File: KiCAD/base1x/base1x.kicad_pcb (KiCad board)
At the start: 4 copper layers, 62.2 x 110 mm, 40 parts, among them J1 Conn_02x05_Odd_Even, J2 GS3, J3 Conn_02x14_Counter_Clockwise, J4 GS3, J6 Conn_02x14_Counter_Clockwise, J7 Conn_02x06_Counter_Clockwise, J8 Conn_02x06_Counter_Clockwise, J9 Screw_Terminal_01x08, P1 CONN_01X02, P2 CONN_01X02, P3 CONN_01X02, P4 CONN_01X02, U1 ADS1115

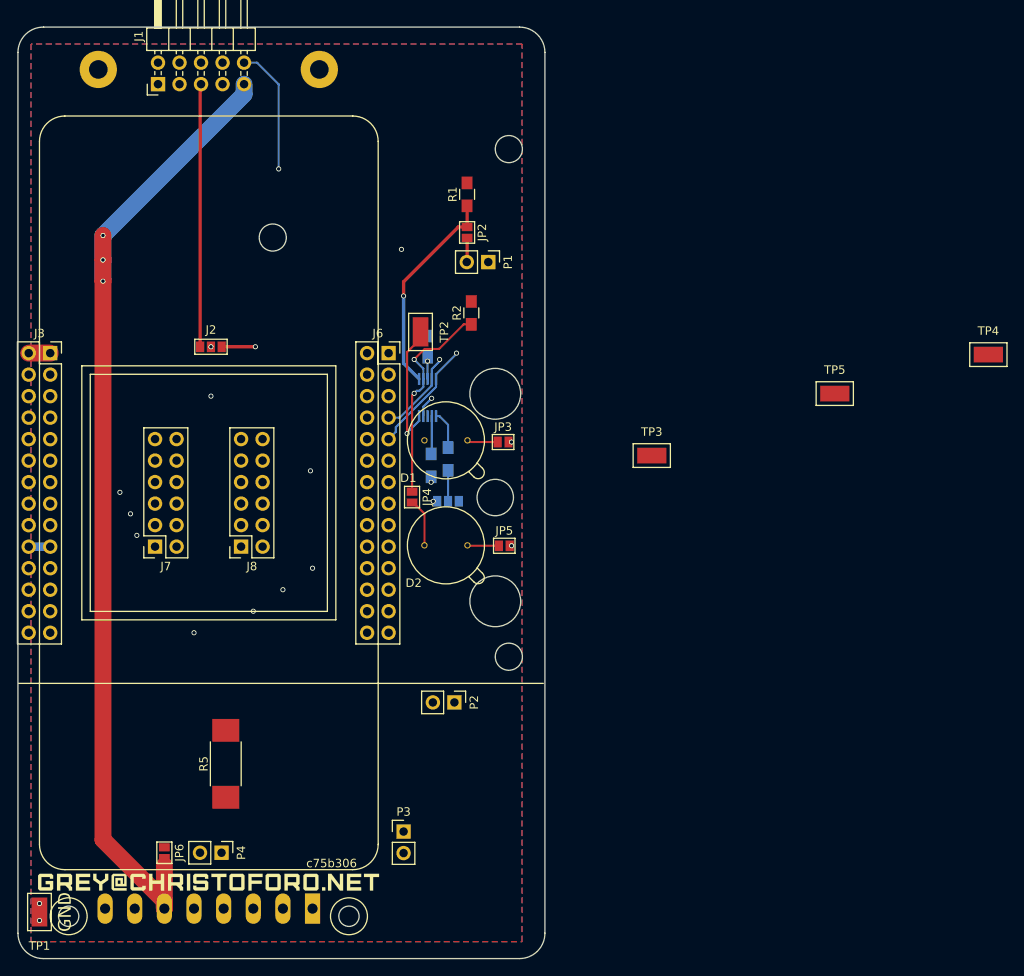
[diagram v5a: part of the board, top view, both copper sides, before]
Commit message: rotate connectors on newMux
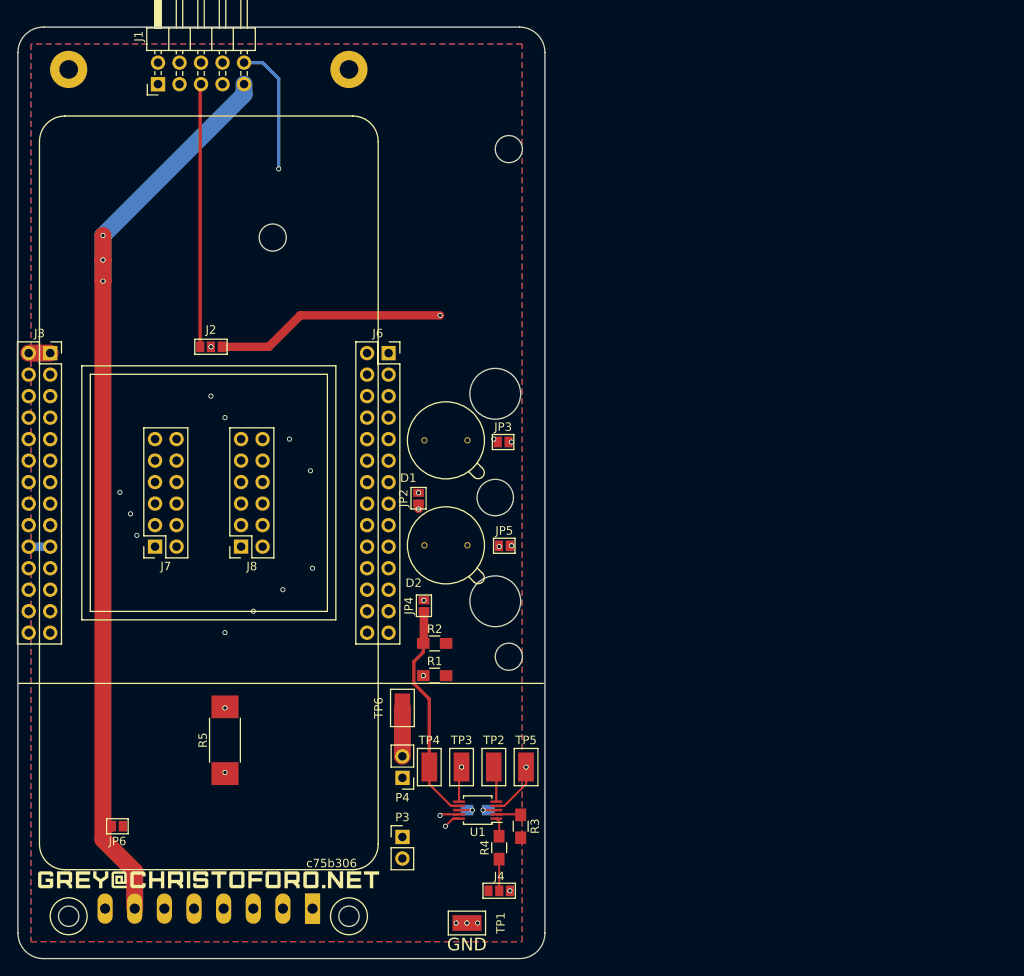
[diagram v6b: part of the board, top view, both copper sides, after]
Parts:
- removed P1, P2: CONN_01X02, Pin_Headers:Pin_Header_Straight_1x02_Pitch2.54mm
- added TP6: Test_Point, myParts:Test_Point_S1751-46R, F.Cu at (22.9, 25.4)
- J4, R3, R4, U1: moved to F.Cu
- moved TP4 82.0 mm to (26.0, 32.4), turned to 90 degrees
- moved TP5 57.2 mm to (37.5, 32.4), turned to 90 degrees
- moved R1 57.0 mm to (26.7, 21.6), turned to 0 degrees
- moved C1 55.0 mm to (31.8, 37.5), turned to 0 degrees
- moved TP2 52.1 mm to (33.7, 32.4), turned to 90 degrees
- moved TP1 50.5 mm to (30.5, 50.8), turned to 180 degrees
- moved U1 49.1 mm to (31.8, 37.5), turned to 180 degrees
- moved J4 46.4 mm to (34.3, 47.0), turned to 270 degrees
- moved R4 46.3 mm to (34.3, 41.9)
- moved R3 43.9 mm to (36.8, 39.4)
- moved TP3 43.1 mm to (29.8, 32.4), turned to 90 degrees
- moved R2 39.3 mm to (26.7, 17.8), turned to 0 degrees
- moved JP2 31.9 mm to (24.8, 0.64), turned to 180 degrees
- moved P4 23.1 mm to (22.9, 33.7), turned to 180 degrees
- moved JP4 12.9 mm to (25.4, 13.3), turned to 180 degrees
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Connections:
- net /ANODE_A renamed Net-(D1-Pad1)
- net /ANODE_B renamed Net-(D2-Pad1)
- net /CATHODE_A renamed Net-(D1-Pad2)
- net /CATHODE_B renamed Net-(D2-Pad2)
- TP2 pad 1: I- -> Net-(TP2-Pad1)
- U1 pad 5: I- -> Net-(TP2-Pad1)
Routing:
- net V_D_LOC: track 29.8 -> 92.2 mm
- net I-_EXT: track 0.00 -> 44.3 mm, vias 0 -> 1
- net SCL: track 104.1 -> 143.4 mm
- net SDA: track 95.8 -> 133.8 mm, vias 1 -> 2
- net Net-(D1-Pad2): track 26.0 -> 3.18 mm, vias 0 -> 1
- net Net-(D1-Pad1): track 26.0 -> 6.49 mm, vias 0 -> 1
- net Net-(D2-Pad2): track 23.0 -> 3.81 mm, vias 0 -> 1
- net Net-(D2-Pad1): track 24.7 -> 6.52 mm, vias 0 -> 1
- net Net-(JP2-Pad1): track 24.9 -> 39.1 mm, vias 1 -> 3
- net I-: track 85.3 -> 93.6 mm
- net /Vin: track 118.6 -> 113.2 mm
- net Net-(TP2-Pad1): track 0.00 -> 4.20 mm
- net Net-(R4-Pad2): track 4.53 -> 2.24 mm
- net Net-(R3-Pad1): track 4.49 -> 2.90 mm
- net GND: track 2.54 -> 4.11 mm, vias 4 -> 7
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
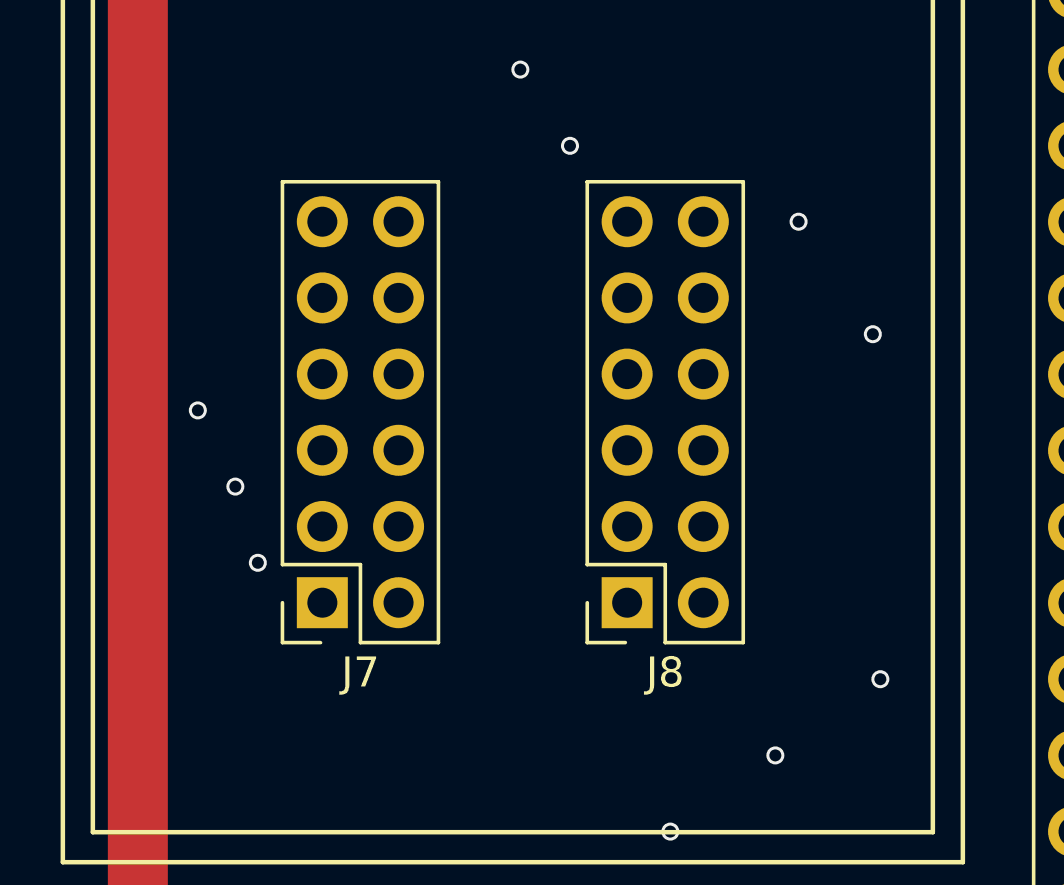
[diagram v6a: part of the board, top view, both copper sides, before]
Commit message: rotate connectors on base1x
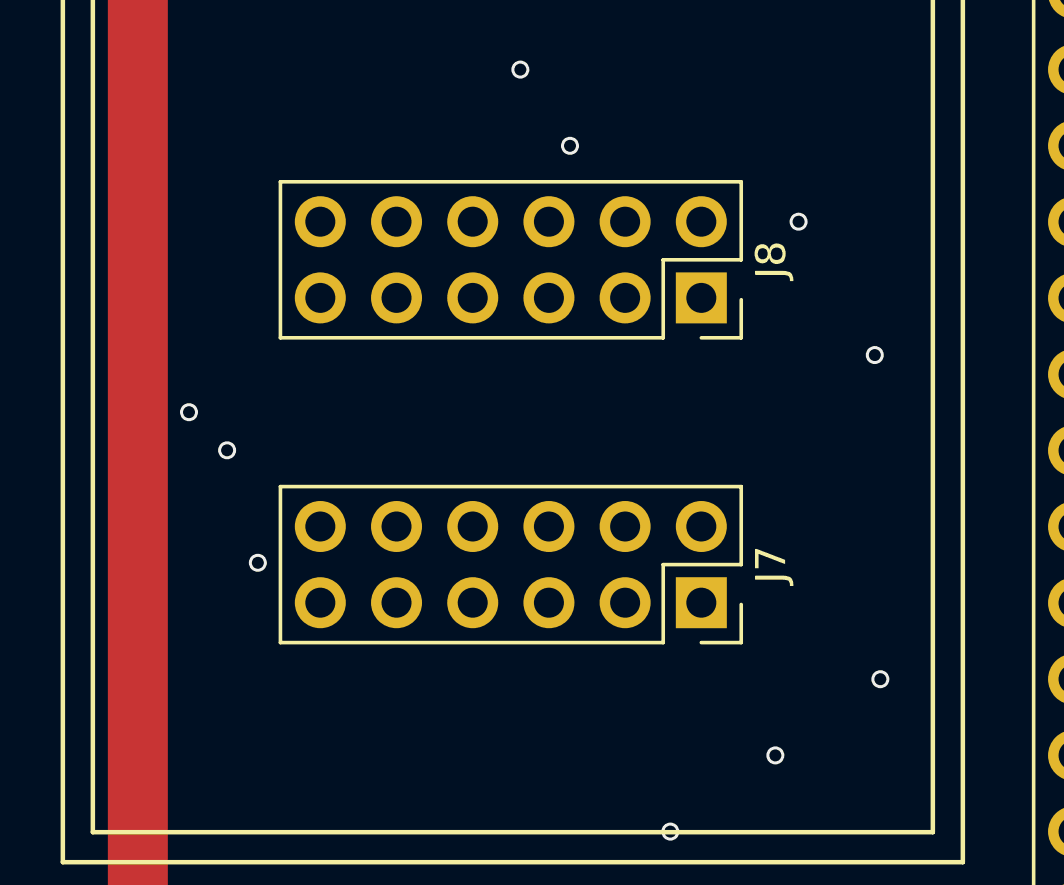
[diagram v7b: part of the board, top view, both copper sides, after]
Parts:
- moved J7 12.6 mm to (6.28, 6.35), turned to 270 degrees
- moved J8 10.5 mm to (6.28, -3.81), turned to 270 degrees
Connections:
- J9 pad 6: Net-(J9-Pad6) -> (no net)
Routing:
- net MOSI: track 99.3 -> 97.1 mm
- net ~CS0: track 91.1 -> 92.4 mm

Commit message: update silk
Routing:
- net SCL: track 143.4 -> 142.5 mm
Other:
- board text added: "3ec2e93"
- board text removed: "c75b306"
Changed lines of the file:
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@@
     (thickness 1.6)
     (drawings 27)
-    (tracks 212)
+    (tracks 210)
     (zones 0)
     (modules 39)
@@
     (pcbplotparams
       (layerselection 0x010fc_ffffffff)
-      (usegerberextensions false)
+      (usegerberextensions true)
       (usegerberattributes true)
       (usegerberadvancedattributes true)
@@
       (xy 8.293997 0.976563) (xy 8.491005 0.779554)) (layer F.SilkS) (width 0.001))
   )
-  (gr_text c75b306 (at 14.5 43.75) (layer F.SilkS)
-    (effects (font (size 1 1) (thickness 0.25)))
+  (gr_text 3ec2e93 (at 13.335 43.18) (layer F.SilkS)
+    (effects (font (size 1.5 1.5) (thickness 0.3)))
   )
   (gr_text GND (at 30.48 53.34) (layer F.SilkS)
@@
   (segment (start -21.27 1.28) (end -18.73 1.28) (width 1) (layer In1.Cu) (net 4))
   (segment (start 21.23 1.28) (end 18.69 1.28) (width 1) (layer In1.Cu) (net 4))
+  (segment (start 8.255 -5.08) (end -7.64 -5.08) (width 0.4) (layer In1.Cu) (net 7))
+  (segment (start -7.64 -5.08) (end -8.9 -6.34) (width 0.4) (layer In1.Cu) (net 7))
+  (segment (start 9.525 -6.35) (end 8.255 -5.08) (width 0.4) (layer In1.Cu) (net 7))
+  (segment (start -18.73 -6.34) (end -8.9 -6.34) (width 1) (layer In1.Cu) (net 7))
+  (segment (start 9.525 -6.35) (end 2.830001 -13.044999) (width 0.4) (layer In2.Cu) (net 7))
+  (segment (start 9.535 -6.34) (end 9.525 -6.35) (width 1) (layer In1.Cu) (net 7))
+  (segment (start 18.69 -6.34) (end 9.535 -6.34) (width 1) (layer In1.Cu) (net 7))
+  (via (at 9.525 -6.35) (size 0.6) (drill 0.4) (layers F.Cu B.Cu) (net 7))
   (segment (start 12.065 -1.905) (end -16.835 -1.905) (width 1) (layer In1.Cu) (net 13))
   (segment (start -16.835 -1.905) (end -18.73 -3.8) (width 1) (layer In1.Cu) (net 13))
@@
   (segment (start 1.62 -50.8) (end 2.830001 -49.589999) (width 0.4) (layer In2.Cu) (net 7))
   (segment (start 2.830001 -49.589999) (end 2.830001 -13.044999) (width 0.4) (layer In2.Cu) (net 7))
-  (segment (start 2.830001 -13.044999) (end 9.225001 -6.649999) (width 0.4) (layer In2.Cu) (net 7))
-  (segment (start 9.225001 -6.649999) (end 9.525 -6.35) (width 0.4) (layer In2.Cu) (net 7))
-  (via (at 9.525 -6.35) (size 0.6) (drill 0.4) (layers F.Cu B.Cu) (net 7))
   (segment (start 1.62 -48.26) (end 1.62 -9.165) (width 0.4) (layer In2.Cu) (net 6))
   (segment (start 1.62 -9.165) (end 1.905 -8.88) (width 0.4) (layer In2.Cu) (net 6))
@@
   (segment (start -18.73 -8.88) (end -21.27 -8.88) (width 1) (layer In1.Cu) (net 6))
   (segment (start 21.23 -8.88) (end 18.69 -8.88) (width 1) (layer In1.Cu) (net 6))
-  (segment (start -10.34 -6.34) (end -9.139999 -5.139999) (width 0.4) (layer In1.Cu) (net 7))
-  (segment (start -9.139999 -5.139999) (end 8.139999 -5.139999) (width 0.4) (layer In1.Cu) (net 7))
-  (segment (start 8.139999 -5.139999) (end 9.34 -6.34) (width 0.4) (layer In1.Cu) (net 7))
-  (segment (start -10.34 -6.34) (end -10 -6) (width 1) (layer In1.Cu) (net 7))
-  (segment (start -18.73 -6.34) (end -10.34 -6.34) (width 1) (layer In1.Cu) (net 7))
-  (segment (start 9.34 -6.34) (end 9 -6) (width 1) (layer In1.Cu) (net 7))
-  (segment (start 18.69 -6.34) (end 9.34 -6.34) (width 1) (layer In1.Cu) (net 7))
   (segment (start -21.27 -6.34) (end -18.73 -6.34) (width 1) (layer In1.Cu) (net 7))
   (segment (start 21.23 -6.34) (end 18.69 -6.34) (width 1) (layer In1.Cu) (net 7))
